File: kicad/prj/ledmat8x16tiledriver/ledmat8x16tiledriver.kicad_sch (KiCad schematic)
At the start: 24 parts, among them J1 Conn_02x08_Top_Bottom, J2 Conn_02x08_Top_Bottom, U2 DMP31D7LDW, U3 DMP31D7LDW, U4 DMP31D7LDW, U5 DMP31D7LDW

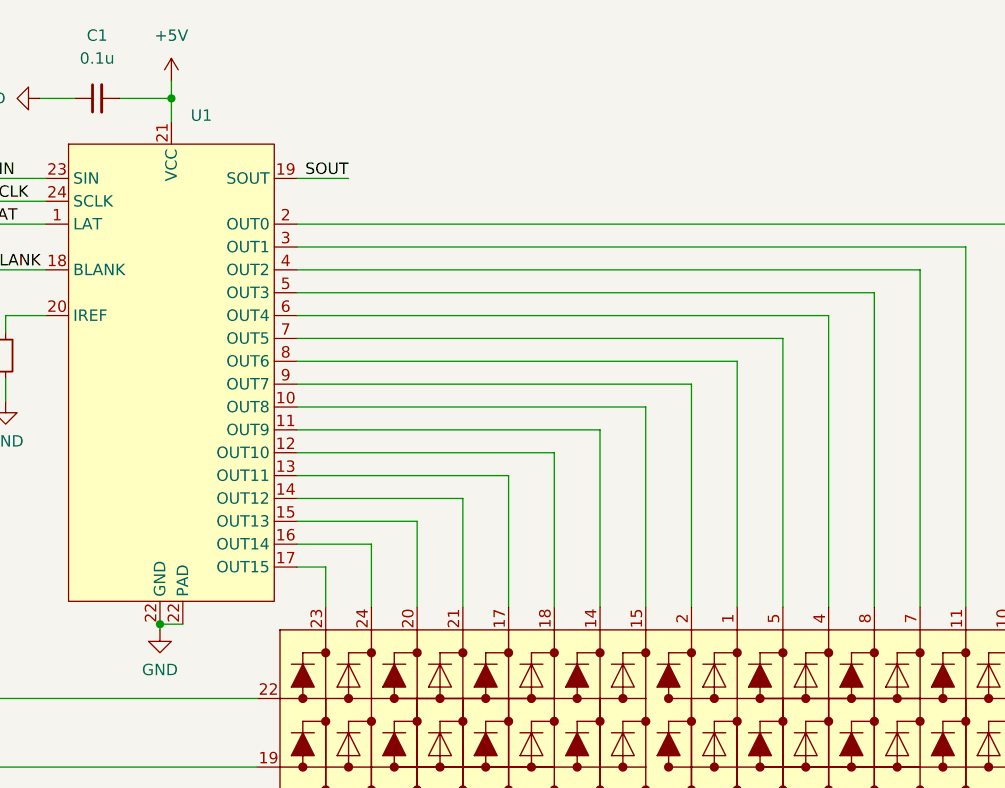
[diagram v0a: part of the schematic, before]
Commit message: create/assign all footprints
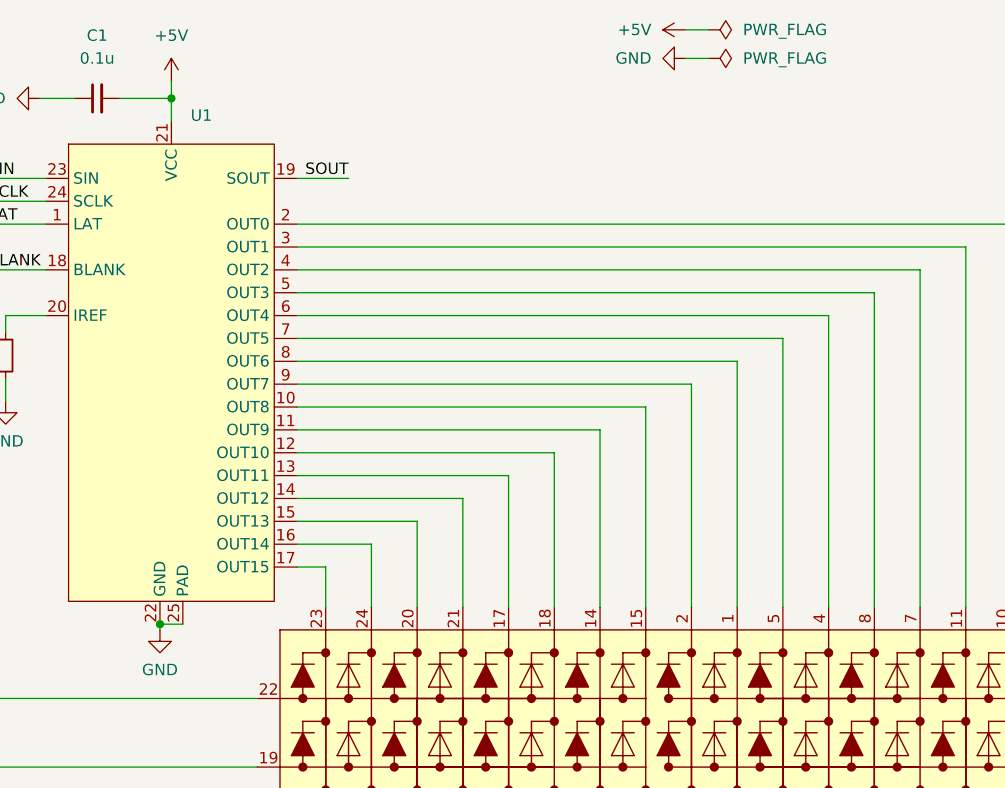
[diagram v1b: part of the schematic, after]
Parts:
- DS1: footprint (none) -> ledmat8x16:LTP-12188M-08
- J1: footprint (none) -> Connector_PinHeader_2.54mm:PinHeader_2x08_P2.54mm_Horizontal
- J2: footprint (none) -> Connector_PinSocket_2.54mm:PinSocket_2x08_P2.54mm_Horizontal
- U2, U3, U4, U5: footprint Package_TO_SOT_SMD:SOT-363_SC-70-6_Handsoldering -> ledmat8x16:SOT-363_SC-70-6_Handsoldering
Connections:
- net GND: now also U1.25 (PAD)

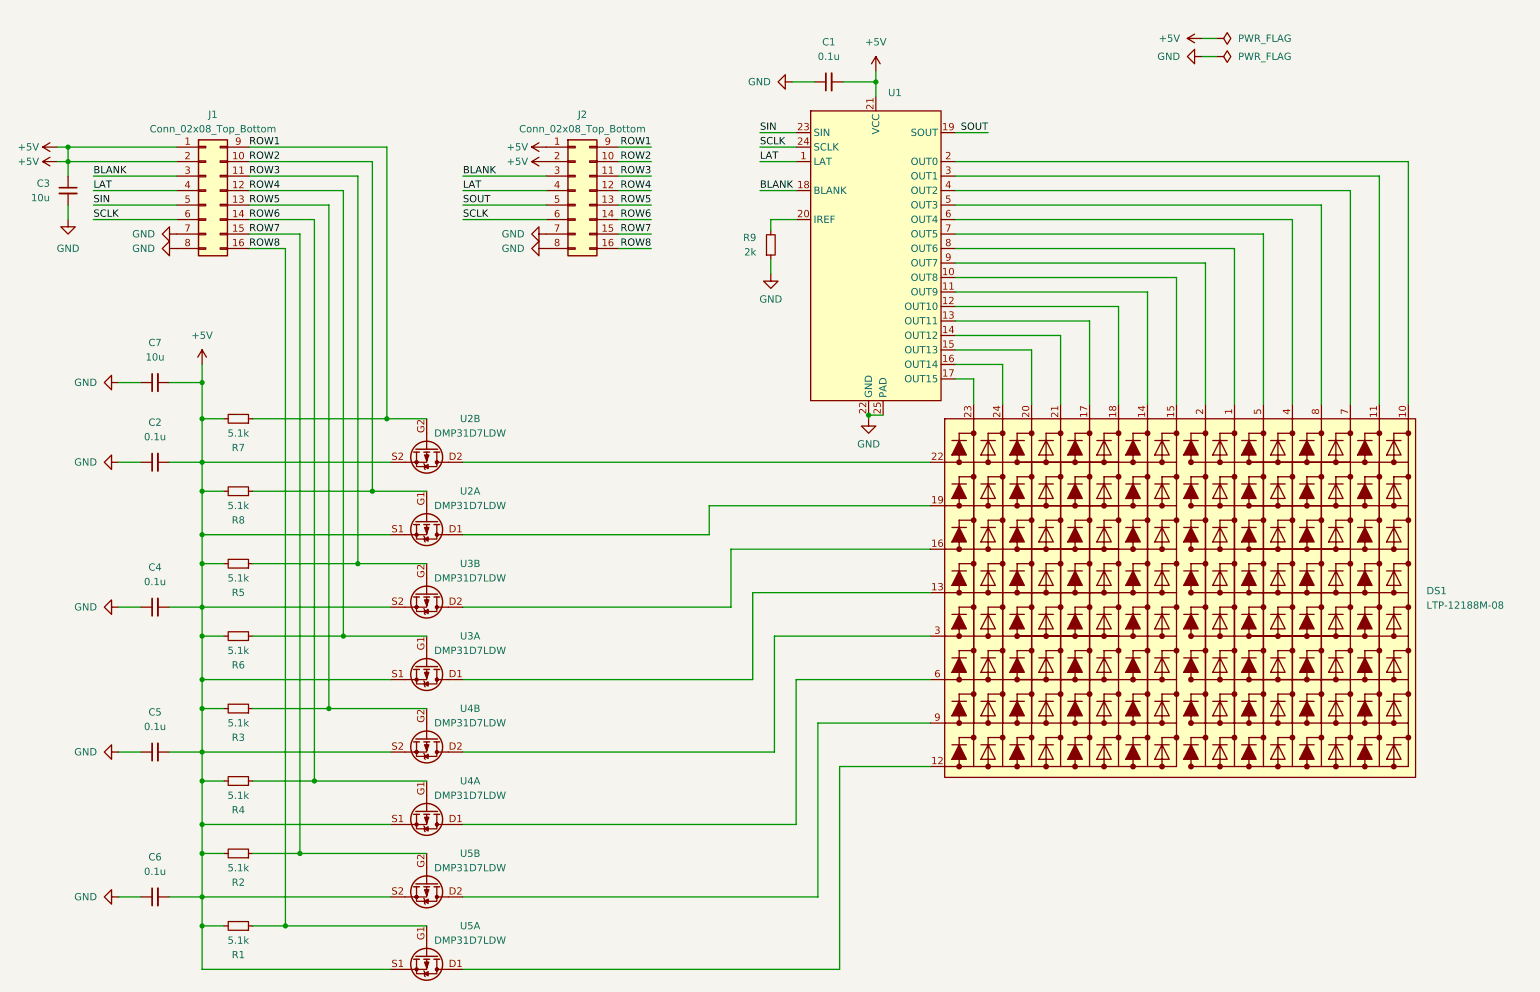
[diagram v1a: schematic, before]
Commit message: finish layout (witch a catch)
I put the led matrix footprint on the wrong side of the board...
This was fixed by moving the pin headers which however now results in
the controller IC being under the led matrix module. Not what I wanted
but not easy to fix. I wanted to use headers to mount the module anyways
to there should be no interference. Try to use some short female pin
headers (which apparently is a thing).
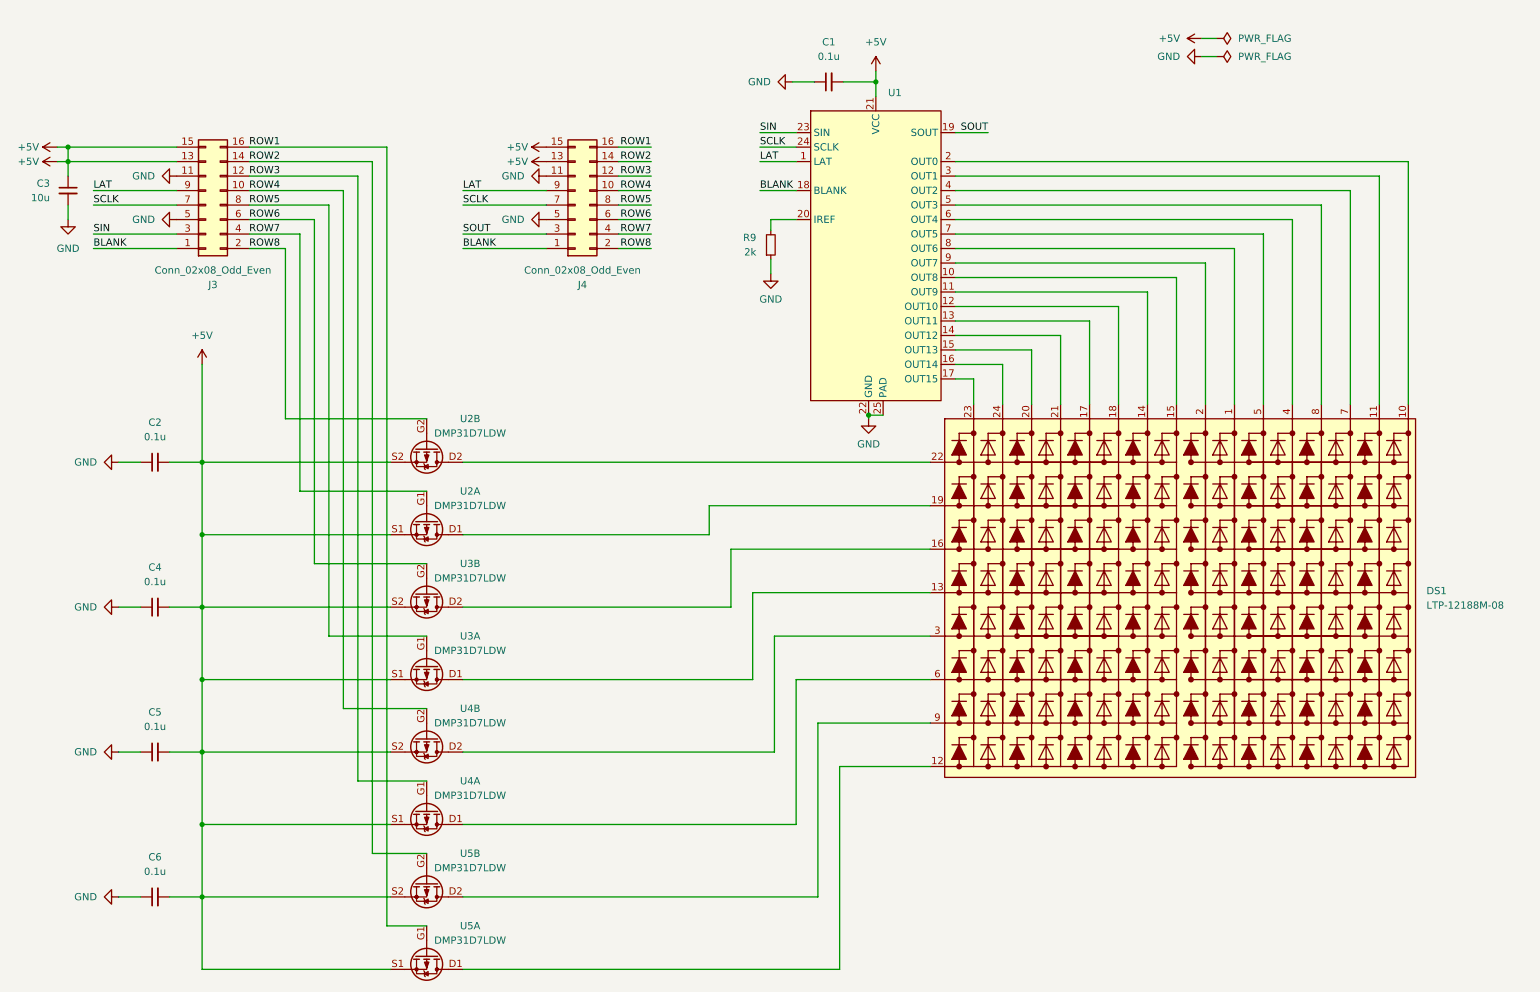
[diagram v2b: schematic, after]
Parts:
- removed C7: 10u, Capacitor_SMD:C_0805_2012Metric_Pad1.18x1.45mm_HandSolder, symbol Device:C_Small
- removed J1: Conn_02x08_Top_Bottom, Connector_PinHeader_2.54mm:PinHeader_2x08_P2.54mm_Horizontal, symbol Connector_Generic:Conn_02x08_Top_Bottom
- removed J2: Conn_02x08_Top_Bottom, Connector_PinSocket_2.54mm:PinSocket_2x08_P2.54mm_Horizontal, symbol Connector_Generic:Conn_02x08_Top_Bottom
- removed R1, R2, R3, R4, R5, R6, R7, R8: 5.1k, Resistor_SMD:R_0603_1608Metric_Pad0.98x0.95mm_HandSolder, symbol Device:R_Small
- added J3: Conn_02x08_Odd_Even, Connector_PinHeader_2.54mm:PinHeader_2x08_P2.54mm_Horizontal, symbol Connector_Generic:Conn_02x08_Odd_Even
- added J4: Conn_02x08_Odd_Even, Connector_PinSocket_2.54mm:PinSocket_2x08_P2.54mm_Horizontal, symbol Connector_Generic:Conn_02x08_Odd_Even
- U1: footprint Package_DFN_QFN:Texas_RGE0024C_VQFN-24-1EP_4x4mm_P0.5mm_EP2.1x2.1mm_ThermalVias -> Package_DFN_QFN:Texas_RGE0024C_VQFN-24-1EP_4x4mm_P0.5mm_EP2.1x2.1mm
- U2, U3, U4, U5: footprint ledmat8x16:SOT-363_SC-70-6_Handsoldering -> ledmat8x16:SOT-363_SC-70-6
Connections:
- net +5V: now also J3.13 (Pin_13), J3.15 (Pin_15), J4.13 (Pin_13), J4.15 (Pin_15)
- net BLANK: now also J3.1 (Pin_1), J4.1 (Pin_1)
- net GND: now also J3.11 (Pin_11), J3.5 (Pin_5), J4.11 (Pin_11), J4.5 (Pin_5)
- net LAT: now also J3.9 (Pin_9), J4.9 (Pin_9)
- net ROW1: now also U5.G1, J3.16 (Pin_16), J4.16 (Pin_16); no longer U2.G2
- net ROW2: now also U5.G2, J3.14 (Pin_14), J4.14 (Pin_14); no longer U2.G1
- net ROW3: now also U4.G1, J3.12 (Pin_12), J4.12 (Pin_12); no longer U3.G2
- net ROW4: now also U4.G2, J3.10 (Pin_10), J4.10 (Pin_10); no longer U3.G1
- net ROW5: now also U3.G1, J3.8 (Pin_8), J4.8 (Pin_8); no longer U4.G2
- net ROW6: now also U3.G2, J3.6 (Pin_6), J4.6 (Pin_6); no longer U4.G1
- net ROW7: now also U2.G1, J3.4 (Pin_4), J4.4 (Pin_4); no longer U5.G2
- net ROW8: now also U2.G2, J3.2 (Pin_2), J4.2 (Pin_2); no longer U5.G1
- net SCLK: now also J3.7 (Pin_7), J4.7 (Pin_7)
- net SIN: now also J3.3 (Pin_3)
- net SOUT: now also J4.3 (Pin_3)

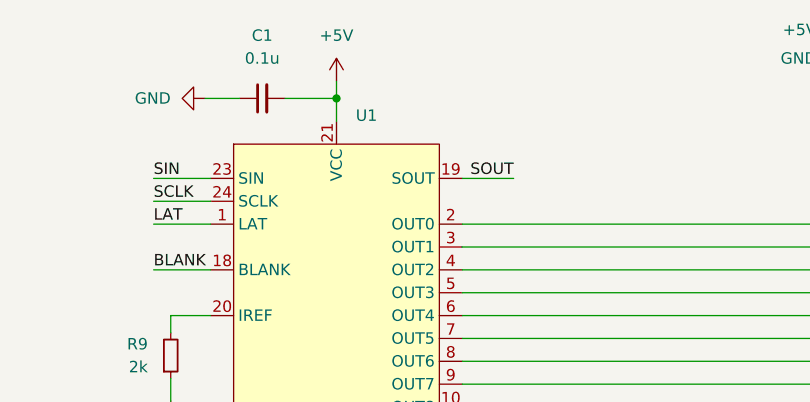
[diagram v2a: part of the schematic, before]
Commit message: Fix empty value field for TLC59283
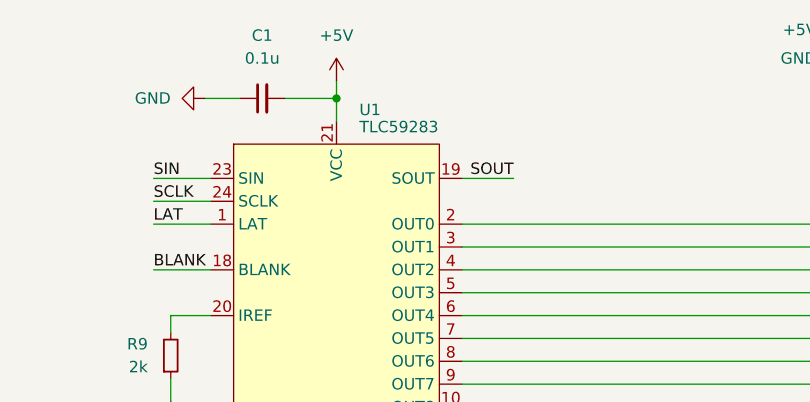
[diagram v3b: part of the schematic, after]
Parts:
- U1: value ~ -> TLC59283
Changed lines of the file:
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@@
 		(on_board yes)
 		(dnp no)
-		(fields_autoplaced yes)
 		(property "Reference" "U1"
-			(at 171.0533 29.21 0)
+			(at 171.45 28.575 0)
 			(effects
 				(font
@@
 			)
 		)
-		(property "Value" "~"
-			(at 171.0533 30.48 0)
+		(property "Value" "TLC59283"
+			(at 171.45 30.48 0)
 			(effects
 				(font

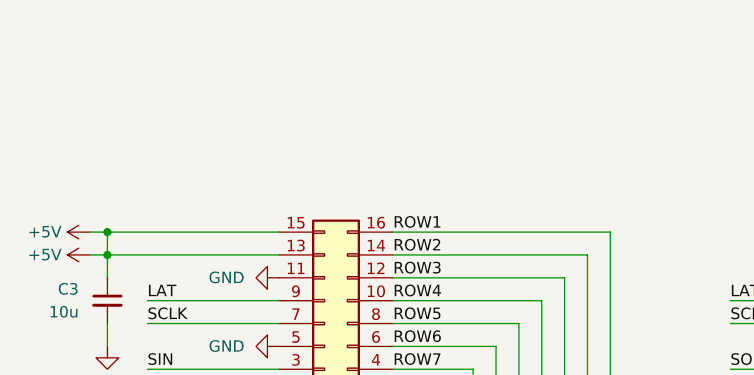
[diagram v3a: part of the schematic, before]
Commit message: Add some holes for headers near the top/bottom edge
Perhaps this can be used as a different way of mounting. Not sure, I'll
have to try. Unfortunately the board dimensions did not allow for the
spacing to be a multiple of 2.54mm. But positioning is such that between
adjacent rows the headers should be exactly 2.54mm apart.
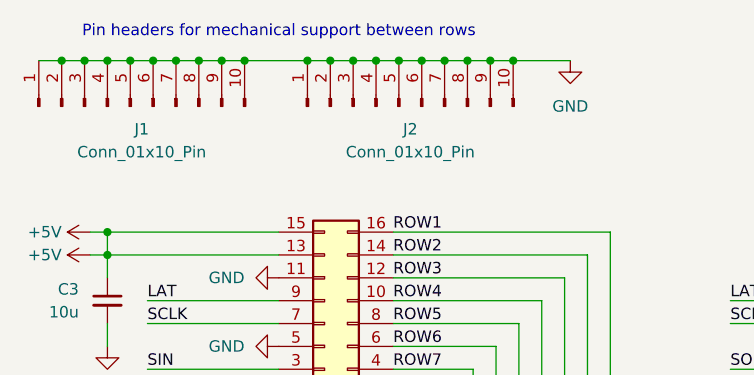
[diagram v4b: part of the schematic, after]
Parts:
- added J1, J2: Conn_01x10_Pin, Connector_PinHeader_2.54mm:PinHeader_1x10_P2.54mm_Vertical, symbol Connector:Conn_01x10_Pin
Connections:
- net GND: now also J1.1 (Pin_1), J1.10 (Pin_10), J1.2 (Pin_2), J1.3 (Pin_3), J1.4 (Pin_4), J1.5 (Pin_5), J1.6 (Pin_6), J1.7 (Pin_7), J1.8 (Pin_8), J1.9 (Pin_9), J2.1 (Pin_1), J2.10 (Pin_10), J2.2 (Pin_2), J2.3 (Pin_3), J2.4 (Pin_4), J2.5 (Pin_5), J2.6 (Pin_6), J2.7 (Pin_7), J2.8 (Pin_8), J2.9 (Pin_9)
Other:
- note added: "Pin headers for mechanical support between rows"
